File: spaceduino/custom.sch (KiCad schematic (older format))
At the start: 10 parts, among them Q4 BC856BS, Q5 BSS84, U8 MPD200A, U9 INA226

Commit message: move more parts to jlcsmt catalog
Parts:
- Q4: LCSC C456122 -> C105896
- Q5: LCSC (none) -> C508197
- U9: LCSC (none) -> C49851
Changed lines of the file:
@@
 F 2 "Package_TO_SOT_SMD:SOT-363_SC-70-6" H 4350 3950 50  0001 C CNN
 F 3 "https://assets.nexperia.com/documents/data-sheet/BC856BS.pdf" H 4150 3850 50  0001 C CNN
-F 4 "C456122" H 4150 3850 50  0001 C CNN "LCSC"
+F 4 "C105896" H 4150 3850 50  0001 C CNN "LCSC"
 	1    4150 3850
 	-1   0    0    1
@@
 F 2 "Package_TO_SOT_SMD:SOT-363_SC-70-6" H 5050 3950 50  0001 C CNN
 F 3 "https://assets.nexperia.com/documents/data-sheet/BC856BS.pdf" H 4850 3850 50  0001 C CNN
-F 4 "C456122" H 4850 3850 50  0001 C CNN "LCSC"
+F 4 "C105896" H 4850 3850 50  0001 C CNN "LCSC"
 	2    4850 3850
 	1    0    0    1
@@
 F 2 "Package_SO:VSSOP-10_3x3mm_P0.5mm" H 6850 2350 50  0001 C CNN
 F 3 "http://www.ti.com/lit/ds/symlink/ina226.pdf" H 6400 2700 50  0001 C CNN
+F 4 "C49851" H 6050 2800 50  0001 C CNN "LCSC"
 	1    6050 2800
 	1    0    0    -1
@@
 F 2 "Package_TO_SOT_SMD:SOT-23" H 4150 2925 50  0001 L CIN
 F 3 "http://assets.nexperia.com/documents/data-sheet/BSS84.pdf" H 3950 3000 50  0001 L CNN
+F 4 "C508197" H 3950 3000 50  0001 C CNN "LCSC"
 	1    3950 3000
 	1    0    0    -1

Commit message: Assigned footprints for SD Card, potentiometer, and resistors
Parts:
- R22, R23, R24, R25, R26: footprint (none) -> Resistor_SMD:R_1206_3216Metric
- RV1: footprint (none) -> Potentiometer_SMD:Potentiometer_ACP_CA14-VSMD_Vertical
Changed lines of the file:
@@
 F 0 "RV1" H 3980 4304 50  0000 R CNN
 F 1 "R_POT" H 3980 4395 50  0000 R CNN
-F 2 "" H 4050 4350 50  0001 C CNN
+F 2 "Potentiometer_SMD:Potentiometer_ACP_CA14-VSMD_Vertical" H 4050 4350 50  0001 C CNN
 F 3 "~" H 4050 4350 50  0001 C CNN
 	1    4050 4350
@@
 F 0 "R25" H 4120 4796 50  0000 L CNN
 F 1 "27" H 4120 4705 50  0000 L CNN
-F 2 "" V 3980 4750 50  0001 C CNN
+F 2 "Resistor_SMD:R_1206_3216Metric" V 3980 4750 50  0001 C CNN
 F 3 "~" H 4050 4750 50  0001 C CNN
 	1    4050 4750
@@
 F 0 "R23" H 4120 3446 50  0000 L CNN
 F 1 "10" H 4120 3355 50  0000 L CNN
-F 2 "" V 3980 3400 50  0001 C CNN
+F 2 "Resistor_SMD:R_1206_3216Metric" V 3980 3400 50  0001 C CNN
 F 3 "~" H 4050 3400 50  0001 C CNN
 	1    4050 3400
@@
 F 0 "R24" H 5020 3446 50  0000 L CNN
 F 1 "10" H 5020 3355 50  0000 L CNN
-F 2 "" V 4880 3400 50  0001 C CNN
+F 2 "Resistor_SMD:R_1206_3216Metric" V 4880 3400 50  0001 C CNN
 F 3 "~" H 4950 3400 50  0001 C CNN
 	1    4950 3400
@@
 F 0 "R22" H 5020 3046 50  0000 L CNN
 F 1 "50m" H 5020 2955 50  0000 L CNN
-F 2 "" V 4880 3000 50  0001 C CNN
+F 2 "Resistor_SMD:R_1206_3216Metric" V 4880 3000 50  0001 C CNN
 F 3 "~" H 4950 3000 50  0001 C CNN
 	1    4950 3000
@@
 F 0 "R26" H 4670 3446 50  0000 L CNN
 F 1 "10k" H 4670 3355 50  0000 L CNN
-F 2 "" V 4530 3400 50  0001 C CNN
+F 2 "Resistor_SMD:R_1206_3216Metric" V 4530 3400 50  0001 C CNN
 F 3 "~" H 4600 3400 50  0001 C CNN
 	1    4600 3400

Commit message: spaceduino laid out???
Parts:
- RV1: footprint Potentiometer_SMD:Potentiometer_ACP_CA14-VSMD_Vertical -> Potentiometer_THT:Potentiometer_Bourns_3296Y_Vertical
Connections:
- net a2_exp_en: now reaches Q5.1 (G)
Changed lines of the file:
@@
 F 0 "RV1" H 3980 4304 50  0000 R CNN
 F 1 "R_POT" H 3980 4395 50  0000 R CNN
-F 2 "Potentiometer_SMD:Potentiometer_ACP_CA14-VSMD_Vertical" H 4050 4350 50  0001 C CNN
+F 2 "Potentiometer_THT:Potentiometer_Bourns_3296Y_Vertical" H 4050 4350 50  0001 C CNN
 F 3 "~" H 4050 4350 50  0001 C CNN
 	1    4050 4350
@@
 Wire Wire Line
 	4600 3200 4600 3250
+Text GLabel 3750 3000 0    50   Input ~ 0
+a2_exp_en
 $EndSCHEMATC

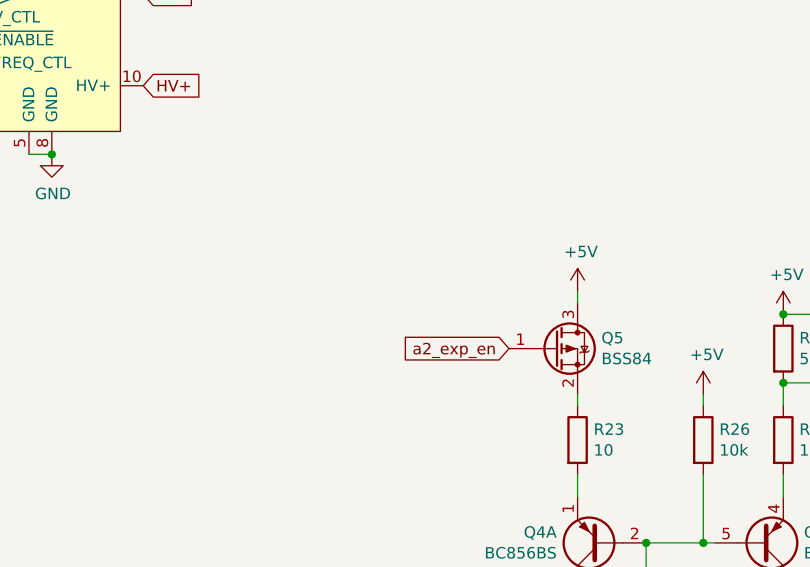
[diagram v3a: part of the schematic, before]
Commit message: use sd card that is actually in stock on digikey
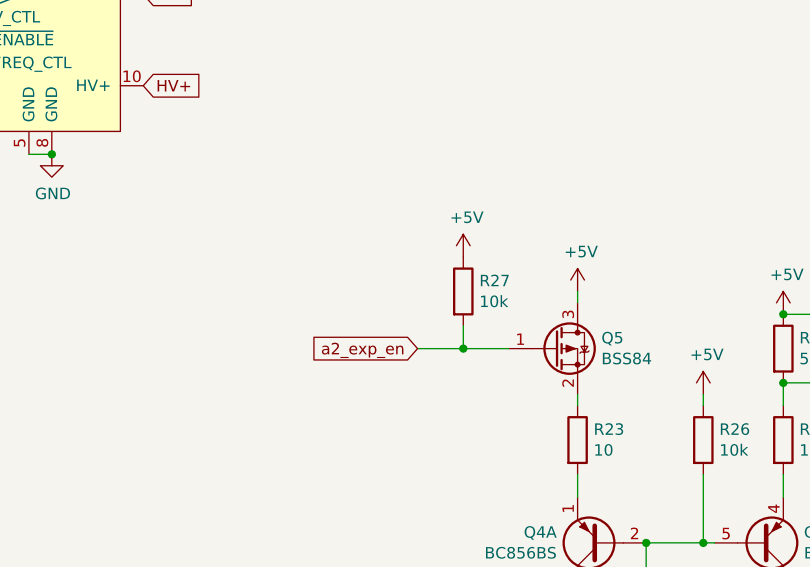
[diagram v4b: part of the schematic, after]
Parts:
- added R27: 10k, Resistor_SMD:R_1206_3216Metric, symbol Device:R
- R22: LCSC (none) -> C601102
- R25: LCSC (none) -> C17946
- R26: LCSC (none) -> C17902
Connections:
- net +5V: now also R27.1
- net a2_exp_en: now also R27.2
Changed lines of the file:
@@
 F 2 "Resistor_SMD:R_1206_3216Metric" V 3980 4750 50  0001 C CNN
 F 3 "~" H 4050 4750 50  0001 C CNN
+F 4 "C17946" H 4050 4750 50  0001 C CNN "LCSC"
 	1    4050 4750
 	1    0    0    -1
@@
 F 2 "Resistor_SMD:R_1206_3216Metric" V 4880 3000 50  0001 C CNN
 F 3 "~" H 4950 3000 50  0001 C CNN
+F 4 "C601102" H 4950 3000 50  0001 C CNN "LCSC"
 	1    4950 3000
 	1    0    0    -1
@@
 F 2 "Resistor_SMD:R_1206_3216Metric" V 4530 3400 50  0001 C CNN
 F 3 "~" H 4600 3400 50  0001 C CNN
+F 4 "C17902" H 4600 3400 50  0001 C CNN "LCSC"
 	1    4600 3400
 	1    0    0    -1
@@
 Wire Wire Line
 	4600 3200 4600 3250
-Text GLabel 3750 3000 0    50   Input ~ 0
+Text GLabel 3350 3000 0    50   Input ~ 0
 a2_exp_en
+Wire Wire Line
+	3350 3000 3550 3000
+Wire Wire Line
+	3550 3000 3550 2900
+Connection ~ 3550 3000
+Wire Wire Line
+	3550 3000 3750 3000
+$Comp
+L Device:R R27
+U 1 1 6059D693
+P 3550 2750
+F 0 "R27" H 3620 2796 50  0000 L CNN
+F 1 "10k" H 3620 2705 50  0000 L CNN
+F 2 "Resistor_SMD:R_1206_3216Metric" V 3480 2750 50  0001 C CNN
+F 3 "~" H 3550 2750 50  0001 C CNN
+F 4 "C17902" H 3550 2750 50  0001 C CNN "LCSC"
+	1    3550 2750
+	1    0    0    -1
+$EndComp
+$Comp
+L power:+5V #PWR0123
+U 1 1 6059DFA1
+P 3550 2600
+F 0 "#PWR0123" H 3550 2450 50  0001 C CNN
+F 1 "+5V" H 3565 2773 50  0000 C CNN
+F 2 "" H 3550 2600 50  0001 C CNN
+F 3 "" H 3550 2600 50  0001 C CNN
+	1    3550 2600
+	1    0    0    -1
+$EndComp
 $EndSCHEMATC

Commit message: can i get a go dawgs
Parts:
- R22: LCSC C601102 -> C201301
- R23, R24: LCSC (none) -> C17903
- R26: LCSC C17902 -> (none)
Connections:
- net +5V: now also R23.1; no longer R22.1, U9.10 (Vin+)
- net a3_pump_en: now also R26.2
- net at Q4.2 (B1), Q4.5 (B2), Q4.6 (C1)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: no longer R26.2
- net at Q5.2 (S): now also R22.1, U9.10 (Vin+); no longer R23.1
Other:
- moved on the sheet: Q5, R27
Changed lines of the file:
@@
 	1750 2150 1650 2150
 Connection ~ 1750 2150
-Text GLabel 1350 1650 0    50   Input ~ 0
+Text GLabel 1100 1650 0    50   Input ~ 0
 a3_pump_en
 Text GLabel 2150 1450 2    50   Input ~ 0
@@
 Wire Wire Line
 	4050 4100 4050 4050
-Wire Wire Line
-	4350 3850 4600 3850
 Connection ~ 4350 3850
 $Comp
@@
 F 2 "Resistor_SMD:R_1206_3216Metric" V 3980 3400 50  0001 C CNN
 F 3 "~" H 4050 3400 50  0001 C CNN
+F 4 "C17903" H 4050 3400 50  0001 C CNN "LCSC"
 	1    4050 3400
 	1    0    0    -1
@@
 L power:+5V #PWR0120
 U 1 1 60029717
-P 4050 2750
-F 0 "#PWR0120" H 4050 2600 50  0001 C CNN
-F 1 "+5V" H 4065 2923 50  0000 C CNN
-F 2 "" H 4050 2750 50  0001 C CNN
-F 3 "" H 4050 2750 50  0001 C CNN
-	1    4050 2750
+P 4050 3200
+F 0 "#PWR0120" H 4050 3050 50  0001 C CNN
+F 1 "+5V" H 4065 3373 50  0000 C CNN
+F 2 "" H 4050 3200 50  0001 C CNN
+F 3 "" H 4050 3200 50  0001 C CNN
+	1    4050 3200
 	1    0    0    -1
 $EndComp
@@
 F 2 "Resistor_SMD:R_1206_3216Metric" V 4880 3400 50  0001 C CNN
 F 3 "~" H 4950 3400 50  0001 C CNN
+F 4 "C17903" H 4950 3400 50  0001 C CNN "LCSC"
 	1    4950 3400
 	1    0    0    -1
@@
 F 2 "Resistor_SMD:R_1206_3216Metric" V 4880 3000 50  0001 C CNN
 F 3 "~" H 4950 3000 50  0001 C CNN
-F 4 "C601102" H 4950 3000 50  0001 C CNN "LCSC"
+F 4 "C201301" H 4950 3000 50  0001 C CNN "LCSC"
 	1    4950 3000
 	1    0    0    -1
@@
 L power:+5V #PWR0121
 U 1 1 6002B79E
-P 4950 2850
-F 0 "#PWR0121" H 4950 2700 50  0001 C CNN
-F 1 "+5V" H 4965 3023 50  0000 C CNN
-F 2 "" H 4950 2850 50  0001 C CNN
-F 3 "" H 4950 2850 50  0001 C CNN
-	1    4950 2850
+P 4950 2400
+F 0 "#PWR0121" H 4950 2250 50  0001 C CNN
+F 1 "+5V" H 4965 2573 50  0000 C CNN
+F 2 "" H 4950 2400 50  0001 C CNN
+F 3 "" H 4950 2400 50  0001 C CNN
+	1    4950 2400
 	1    0    0    -1
 $EndComp
@@
 L Transistor_FET:BSS84 Q5
 U 1 1 6003471C
-P 3950 3000
-F 0 "Q5" H 4154 3046 50  0000 L CNN
-F 1 "BSS84" H 4154 2955 50  0000 L CNN
-F 2 "Package_TO_SOT_SMD:SOT-23" H 4150 2925 50  0001 L CIN
-F 3 "http://assets.nexperia.com/documents/data-sheet/BSS84.pdf" H 3950 3000 50  0001 L CNN
-F 4 "C508197" H 3950 3000 50  0001 C CNN "LCSC"
-	1    3950 3000
-	1    0    0    -1
-$EndComp
-Wire Wire Line
-	4050 2800 4050 2750
+P 4850 2650
+F 0 "Q5" H 5054 2696 50  0000 L CNN
+F 1 "BSS84" H 5054 2605 50  0000 L CNN
+F 2 "Package_TO_SOT_SMD:SOT-23" H 5050 2575 50  0001 L CIN
+F 3 "http://assets.nexperia.com/documents/data-sheet/BSS84.pdf" H 4850 2650 50  0001 L CNN
+F 4 "C508197" H 4850 2650 50  0001 C CNN "LCSC"
+	1    4850 2650
+	1    0    0    -1
+$EndComp
+Wire Wire Line
+	4950 2450 4950 2400
 Wire Wire Line
 	4050 3200 4050 3250
-$Comp
-L Device:R R26
-U 1 1 60037548
-P 4600 3400
-F 0 "R26" H 4670 3446 50  0000 L CNN
-F 1 "10k" H 4670 3355 50  0000 L CNN
-F 2 "Resistor_SMD:R_1206_3216Metric" V 4530 3400 50  0001 C CNN
-F 3 "~" H 4600 3400 50  0001 C CNN
-F 4 "C17902" H 4600 3400 50  0001 C CNN "LCSC"
-	1    4600 3400
-	1    0    0    -1
-$EndComp
-Wire Wire Line
-	4600 3550 4600 3850
-Connection ~ 4600 3850
-Wire Wire Line
-	4600 3850 4650 3850
-$Comp
-L power:+5V #PWR0122
-U 1 1 600384AE
-P 4600 3200
-F 0 "#PWR0122" H 4600 3050 50  0001 C CNN
-F 1 "+5V" H 4615 3373 50  0000 C CNN
-F 2 "" H 4600 3200 50  0001 C CNN
-F 3 "" H 4600 3200 50  0001 C CNN
-	1    4600 3200
-	1    0    0    -1
-$EndComp
-Wire Wire Line
-	4600 3200 4600 3250
-Text GLabel 3350 3000 0    50   Input ~ 0
+Text GLabel 4250 2650 0    50   Input ~ 0
 a2_exp_en
 Wire Wire Line
-	3350 3000 3550 3000
-Wire Wire Line
-	3550 3000 3550 2900
-Connection ~ 3550 3000
-Wire Wire Line
-	3550 3000 3750 3000
+	4250 2650 4450 2650
+Wire Wire Line
+	4450 2650 4450 2550
+Connection ~ 4450 2650
+Wire Wire Line
+	4450 2650 4650 2650
 $Comp
 L Device:R R27
 U 1 1 6059D693
-P 3550 2750
-F 0 "R27" H 3620 2796 50  0000 L CNN
-F 1 "10k" H 3620 2705 50  0000 L CNN
-F 2 "Resistor_SMD:R_1206_3216Metric" V 3480 2750 50  0001 C CNN
-F 3 "~" H 3550 2750 50  0001 C CNN
-F 4 "C17902" H 3550 2750 50  0001 C CNN "LCSC"
-	1    3550 2750
+P 4450 2400
+F 0 "R27" H 4520 2446 50  0000 L CNN
+F 1 "10k" H 4520 2355 50  0000 L CNN
+F 2 "Resistor_SMD:R_1206_3216Metric" V 4380 2400 50  0001 C CNN
+F 3 "~" H 4450 2400 50  0001 C CNN
+F 4 "C17902" H 4450 2400 50  0001 C CNN "LCSC"
+	1    4450 2400
 	1    0    0    -1
 $EndComp
@@
 L power:+5V #PWR0123
 U 1 1 6059DFA1
-P 3550 2600
-F 0 "#PWR0123" H 3550 2450 50  0001 C CNN
-F 1 "+5V" H 3565 2773 50  0000 C CNN
-F 2 "" H 3550 2600 50  0001 C CNN
-F 3 "" H 3550 2600 50  0001 C CNN
-	1    3550 2600
-	1    0    0    -1
-$EndComp
+P 4450 2250
+F 0 "#PWR0123" H 4450 2100 50  0001 C CNN
+F 1 "+5V" H 4465 2423 50  0000 C CNN
+F 2 "" H 4450 2250 50  0001 C CNN
+F 3 "" H 4450 2250 50  0001 C CNN
+	1    4450 2250
+	1    0    0    -1
+$EndComp
+Wire Wire Line
+	1100 1650 1200 1650
+Wire Wire Line
+	1200 1650 1200 1500
+Connection ~ 1200 1650
+Wire Wire Line
+	1200 1650 1350 1650
+$Comp
+L Device:R R26
+U 1 1 6055E8F6
+P 1200 1350
+F 0 "R26" H 1270 1396 50  0000 L CNN
+F 1 "10k" H 1270 1305 50  0000 L CNN
+F 2 "Resistor_SMD:R_1206_3216Metric" V 1130 1350 50  0001 C CNN
+F 3 "~" H 1200 1350 50  0001 C CNN
+	1    1200 1350
+	1    0    0    -1
+$EndComp
+$Comp
+L power:+5V #PWR0122
+U 1 1 6055F075
+P 1200 1200
+F 0 "#PWR0122" H 1200 1050 50  0001 C CNN
+F 1 "+5V" H 1215 1373 50  0000 C CNN
+F 2 "" H 1200 1200 50  0001 C CNN
+F 3 "" H 1200 1200 50  0001 C CNN
+	1    1200 1200
+	1    0    0    -1
+$EndComp
+Wire Wire Line
+	4350 3850 4650 3850
 $EndSCHEMATC

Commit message: ordered it supposedly
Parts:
- Q5: LCSC C508197 -> C10487
- R25: footprint Resistor_SMD:R_1206_3216Metric -> Resistor_SMD:R_0603_1608Metric; LCSC C17946 -> C25190
- R26: LCSC (none) -> C17902
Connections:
- net +5V: now also Q5.2 (S); no longer Q5.3 (D)
- net at R22.1, U9.10 (Vin+): now also Q5.3 (D); no longer Q5.2 (S)
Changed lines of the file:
@@
 F 0 "R25" H 4120 4796 50  0000 L CNN
 F 1 "27" H 4120 4705 50  0000 L CNN
-F 2 "Resistor_SMD:R_1206_3216Metric" V 3980 4750 50  0001 C CNN
+F 2 "Resistor_SMD:R_0603_1608Metric" V 3980 4750 50  0001 C CNN
 F 3 "~" H 4050 4750 50  0001 C CNN
-F 4 "C17946" H 4050 4750 50  0001 C CNN "LCSC"
+F 4 "C25190" H 4050 4750 50  0001 C CNN "LCSC"
 	1    4050 4750
 	1    0    0    -1
@@
 F 2 "Package_TO_SOT_SMD:SOT-23" H 5050 2575 50  0001 L CIN
 F 3 "http://assets.nexperia.com/documents/data-sheet/BSS84.pdf" H 4850 2650 50  0001 L CNN
-F 4 "C508197" H 4850 2650 50  0001 C CNN "LCSC"
+F 4 "C10487" H 4850 2650 50  0001 C CNN "LCSC"
 	1    4850 2650
-	1    0    0    -1
+	1    0    0    1
 $EndComp
 Wire Wire Line
@@
 F 2 "Resistor_SMD:R_1206_3216Metric" V 1130 1350 50  0001 C CNN
 F 3 "~" H 1200 1350 50  0001 C CNN
+F 4 "C17902" H 1200 1350 50  0001 C CNN "LCSC"
 	1    1200 1350
 	1    0    0    -1
